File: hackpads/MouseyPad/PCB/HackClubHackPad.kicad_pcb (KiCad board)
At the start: 2 copper layers, 60 x 50 mm, 7 parts, among them J1 Conn_01x04, SW1 SW_Push, SW2 SW_Push, SW3 SW_Push, SW4 RotaryEncoder_Switch, SW5 RotaryEncoder_Switch, U1 Seeed Studio XIAO SAMD21

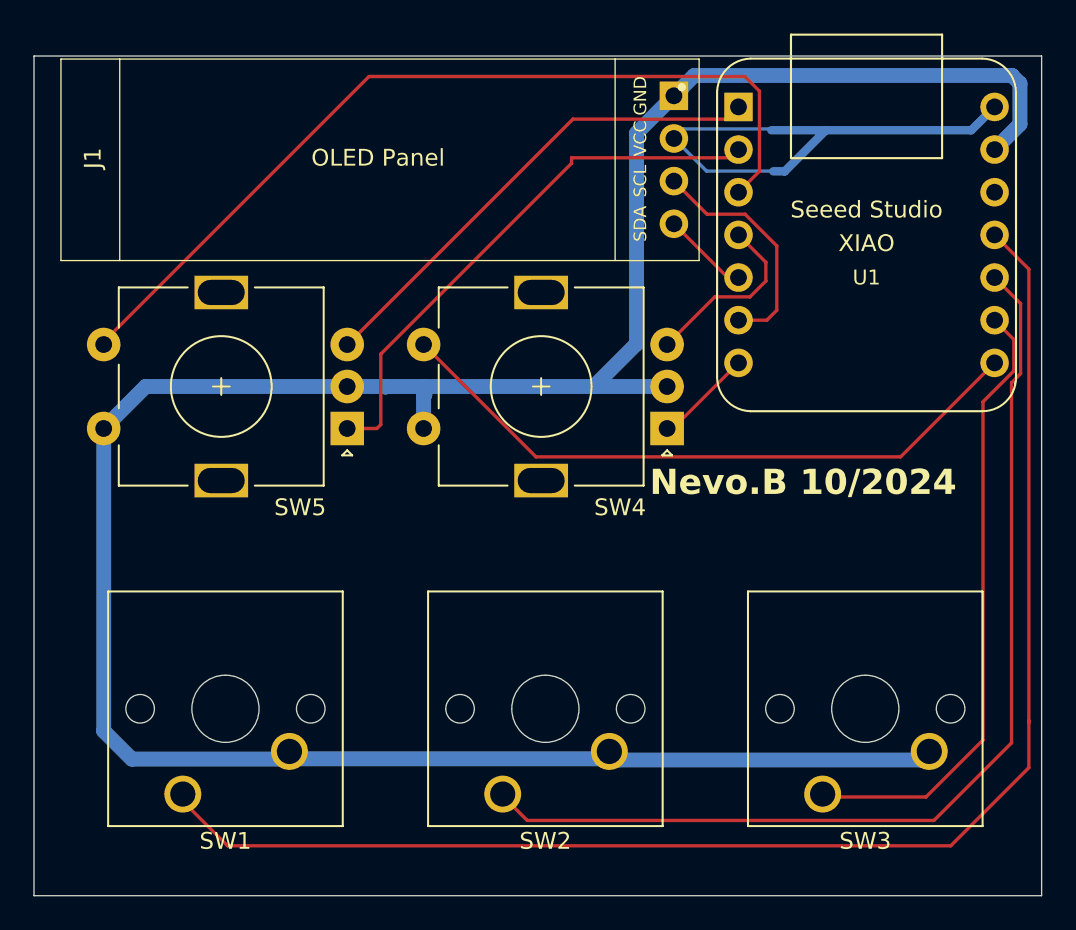
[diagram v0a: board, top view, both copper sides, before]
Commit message: Added LEDs
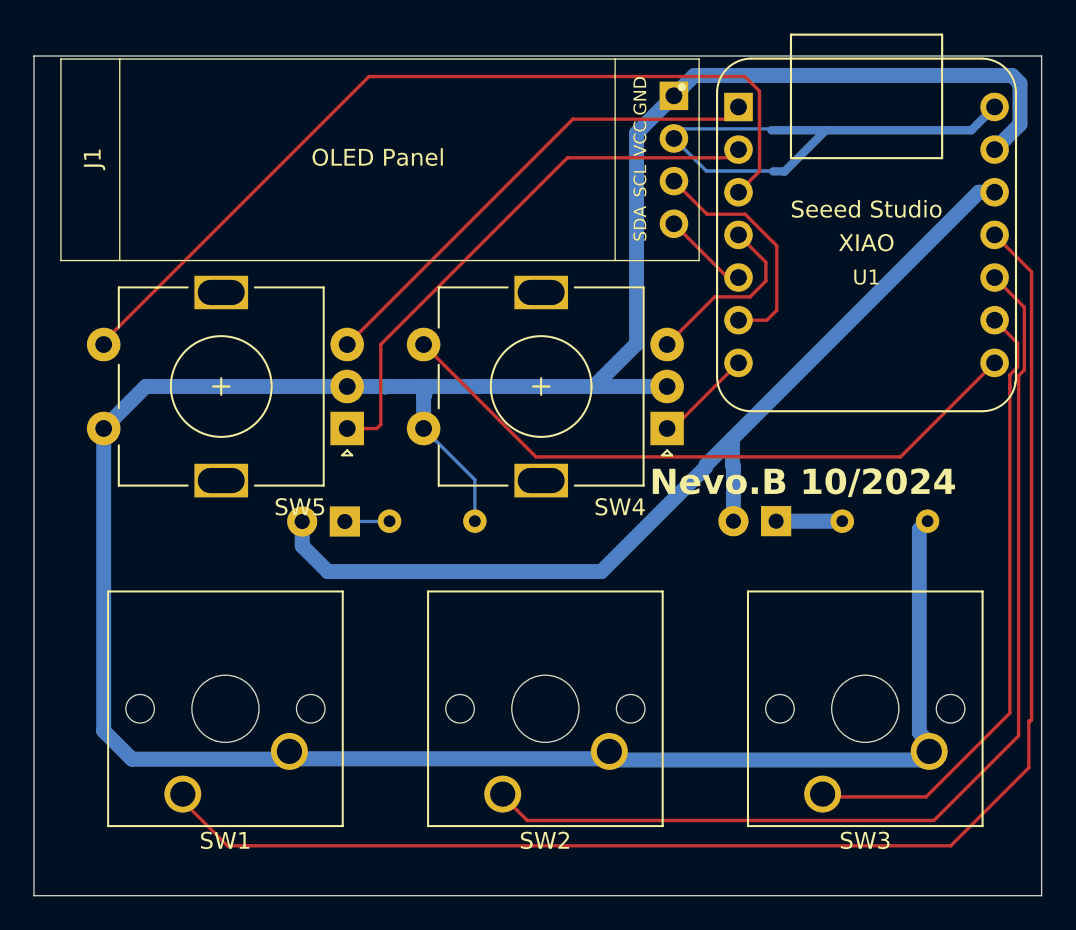
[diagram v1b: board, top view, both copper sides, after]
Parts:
- added D1: LED, LED_THT:LED_D1.8mm_W3.3mm_H2.4mm, B.Cu at (173.3, 50.5)
- added D2: LED, LED_THT:LED_D1.8mm_W3.3mm_H2.4mm, B.Cu at (147.6, 50.5)
- added R1: 36, Resistor_THT:R_Axial_DIN0204_L3.6mm_D1.6mm_P5.08mm_Horizontal, B.Cu at (177.2, 50.5)
- added R2: 36, Resistor_THT:R_Axial_DIN0204_L3.6mm_D1.6mm_P5.08mm_Horizontal, B.Cu at (150.2, 50.5)
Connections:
- net Net-(U1-PA02_A0_D0) renamed EC11B
- net Net-(U1-PA10_A2_D2) renamed EC11SW
- net Net-(U1-PA11_A3_D3) renamed EC11(2)B
- net Net-(U1-PA4_A1_D1) renamed EC11A
- net Net-(U1-PA5_A9_D9_MISO) renamed SW2
- net Net-(U1-PA6_A10_D10_MOSI) renamed SW1
- net Net-(U1-PA7_A8_D8_SCK) renamed SW3
- net Net-(U1-PB08_A6_D6_TX) renamed EC11(2)A
- net Net-(U1-PB09_A7_D7_RX) renamed EC11(2)SW
- U1 pad 12: unconnected-(U1-3V3-Pad12) -> +3.3V
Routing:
- net +3.3V: track 0.00 -> 57.7 mm
- net GND: track 151.3 -> 172.7 mm
- net Net-(D1-K): track 0.00 -> 3.94 mm
- net Net-(D2-K): track 0.00 -> 2.67 mm
